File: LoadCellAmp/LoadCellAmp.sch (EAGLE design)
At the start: 19 parts, among them IC1 AD623RM

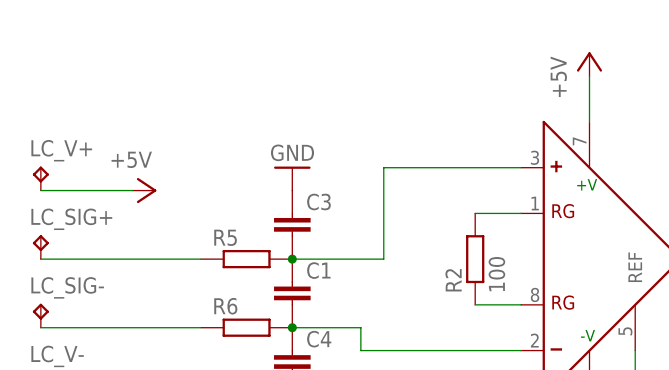
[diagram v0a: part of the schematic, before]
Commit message: Added marker, rearranged silkscreen
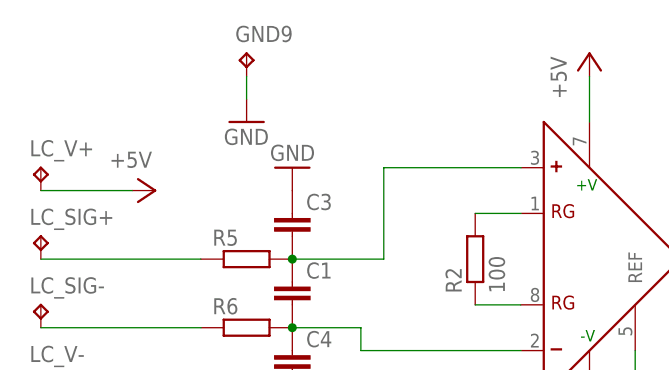
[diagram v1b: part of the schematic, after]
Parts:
- added GND9: TPB1,27, testpad:TPB1,27
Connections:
- net GND: now also GND9.TP
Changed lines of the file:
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@@
 <part name="C5" library="resistor" deviceset="C-EU" device="C0805"/>
 <part name="GND8" library="supply1" deviceset="GND" device=""/>
+<part name="GND9" library="testpad" deviceset="TP" device="B1,27"/>
+<part name="GND10" library="supply1" deviceset="GND" device=""/>
 </parts>
 <sheets>
@@
 <instance part="C5" gate="G$1" x="81.28" y="53.34" rot="R90"/>
 <instance part="GND8" gate="1" x="73.66" y="50.8"/>
+<instance part="GND9" gate="G$1" x="0" y="66.04"/>
+<instance part="GND10" gate="1" x="0" y="58.42"/>
 </instances>
 <busses>
@@
 <wire x1="78.74" y1="53.34" x2="73.66" y2="53.34" width="0.1524" layer="91"/>
 </segment>
+<segment>
+<pinref part="GND9" gate="G$1" pin="TP"/>
+<pinref part="GND10" gate="1" pin="GND"/>
+<wire x1="0" y1="60.96" x2="0" y2="63.5" width="0.1524" layer="91"/>
+</segment>
 </net>

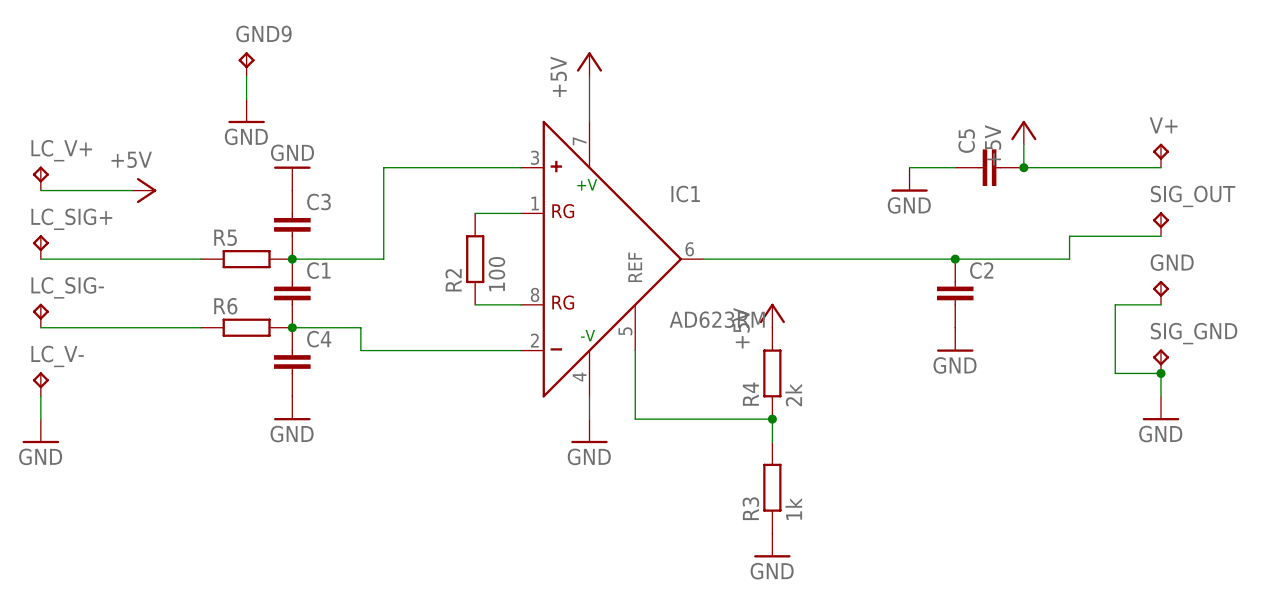
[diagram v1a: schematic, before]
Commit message: Chenged values of R and C.
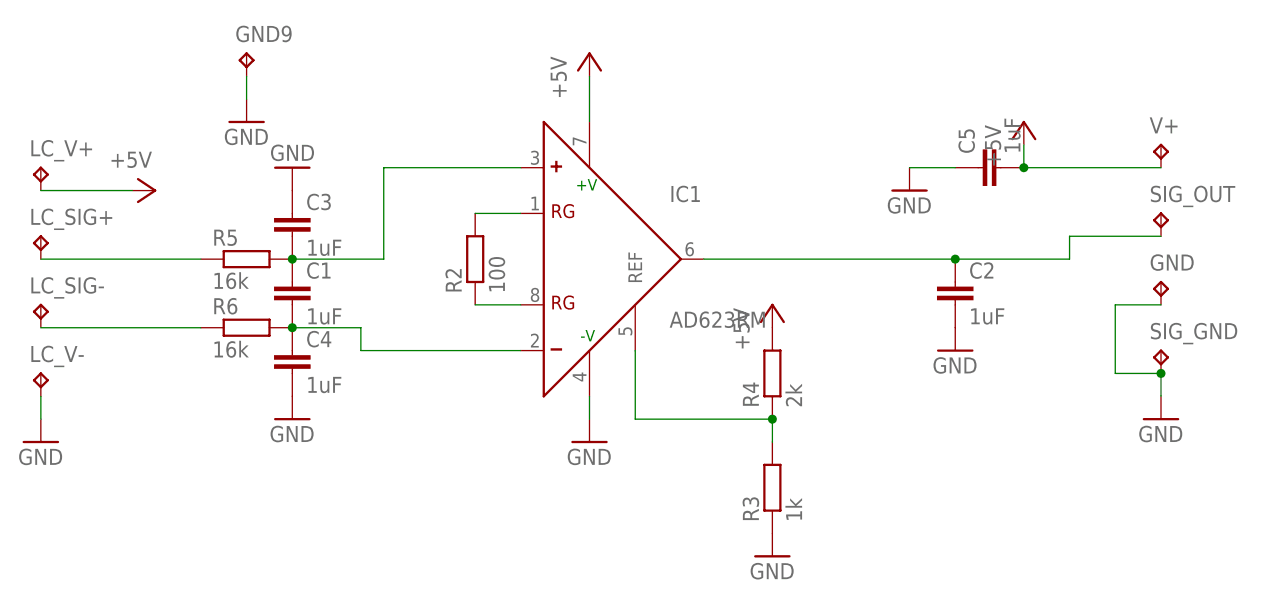
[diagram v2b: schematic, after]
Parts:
- C1, C2, C3, C4, C5: value (none) -> 1uF
- R5, R6: value (none) -> 16k
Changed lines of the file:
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@@
 <parts>
 <part name="IC1" library="analog-devices" deviceset="AD623" device="RM"/>
-<part name="C1" library="resistor" deviceset="C-EU" device="C0805"/>
+<part name="C1" library="resistor" deviceset="C-EU" device="C0805" value="1uF"/>
 <part name="R2" library="rcl" deviceset="R-EU_" device="R0805" value="100"/>
 <part name="LC_V+" library="testpad" deviceset="TP" device="B1,27"/>
@@
 <part name="GND3" library="supply1" deviceset="GND" device=""/>
 <part name="P+4" library="supply1" deviceset="+5V" device=""/>
-<part name="C2" library="resistor" deviceset="C-EU" device="C0805"/>
+<part name="C2" library="resistor" deviceset="C-EU" device="C0805" value="1uF"/>
 <part name="GND4" library="supply1" deviceset="GND" device=""/>
-<part name="R5" library="rcl" deviceset="R-EU_" device="R0805"/>
-<part name="R6" library="rcl" deviceset="R-EU_" device="R0805"/>
-<part name="C3" library="resistor" deviceset="C-EU" device="C0805"/>
-<part name="C4" library="resistor" deviceset="C-EU" device="C0805"/>
+<part name="R5" library="rcl" deviceset="R-EU_" device="R0805" value="16k"/>
+<part name="R6" library="rcl" deviceset="R-EU_" device="R0805" value="16k"/>
+<part name="C3" library="resistor" deviceset="C-EU" device="C0805" value="1uF"/>
+<part name="C4" library="resistor" deviceset="C-EU" device="C0805" value="1uF"/>
 <part name="GND5" library="supply1" deviceset="GND" device=""/>
 <part name="GND6" library="supply1" deviceset="GND" device=""/>
 <part name="GND7" library="supply1" deviceset="GND" device=""/>
-<part name="C5" library="resistor" deviceset="C-EU" device="C0805"/>
+<part name="C5" library="resistor" deviceset="C-EU" device="C0805" value="1uF"/>
 <part name="GND8" library="supply1" deviceset="GND" device=""/>
 <part name="GND9" library="testpad" deviceset="TP" device="B1,27"/>
